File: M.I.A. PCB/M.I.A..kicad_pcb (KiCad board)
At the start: 4 copper layers, 50.8 x 106.6 mm, 177 parts, among them J1 USB_C_Receptacle_USB2.0_16P, J10 Conn_01x03, J11 Conn_01x03, J12 Screw_Terminal_01x02, J13 Screw_Terminal_01x02, J14 Screw_Terminal_01x02, J15 Screw_Terminal_01x02, J16 Screw_Terminal_01x02, J17 Screw_Terminal_01x02, J18 Screw_Terminal_01x02, J19 Conn_01x08_Socket, J2 Conn_01x02_Pin, J20 Screw_Terminal_01x02, J21 Conn_01x04_Socket, J22 Conn_01x04_Socket, J23 Conn_01x04_Socket, J24 Conn_01x04_Socket, J25 Conn_01x04_Socket, J26 Conn_01x02_Socket, J27 Conn_01x02_Socket, J28 Conn_01x02_Socket, J29 Conn_01x02_Socket, J3 Conn_01x03, J30 Conn_01x04_Socket, J31 Conn_01x04_Socket, J32 Conn_01x04_Socket, J33 Conn_Coaxial, J4 Conn_01x03, J5 Conn_01x03, J6 Conn_01x03, J7 MSD-4-A, J8 Conn_01x03, J9 Conn_01x03, Q1 AO3400A, Q2 AO3400A, Q3 AO3400A, Q4 AO3400A, SW1 SW_Push, SW2 SW_Push, U1 W25Q128JVS, U10 AP2112K-3.3, U11 INA219AxDCN, U12 AP62150WU, U13 TPS2121RUXR, U14 AP62150WU, U15 74AHC541, U2 RP2350B-QFN80, U3 MMC5983MA, U4 ICM-45686, U5 MS5611-01BA, U6 TMP117xxDRV, U7 MAX-M10S, U8 KX134-1211, U9 TPS2121RUXR, Y1 ABM8-272-T3

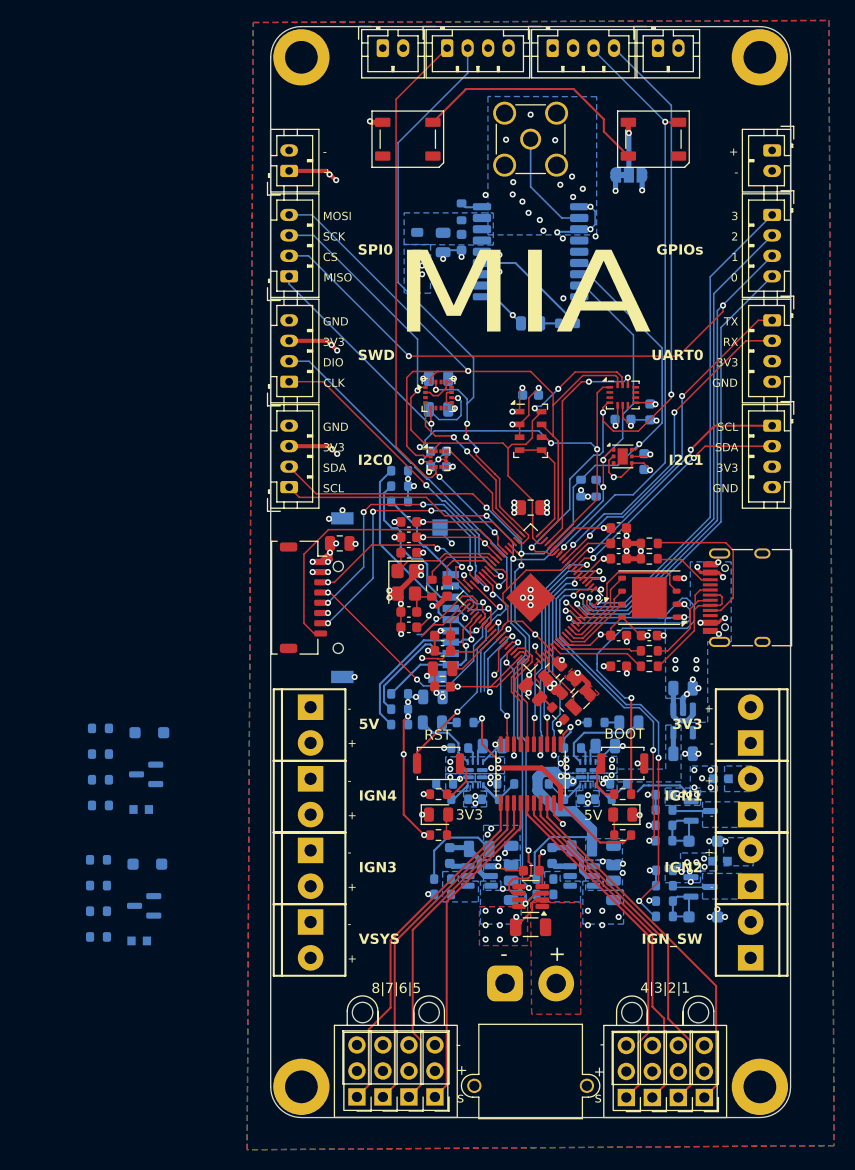
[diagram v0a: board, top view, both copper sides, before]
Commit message: Updated top connectors to be TLM_SPI
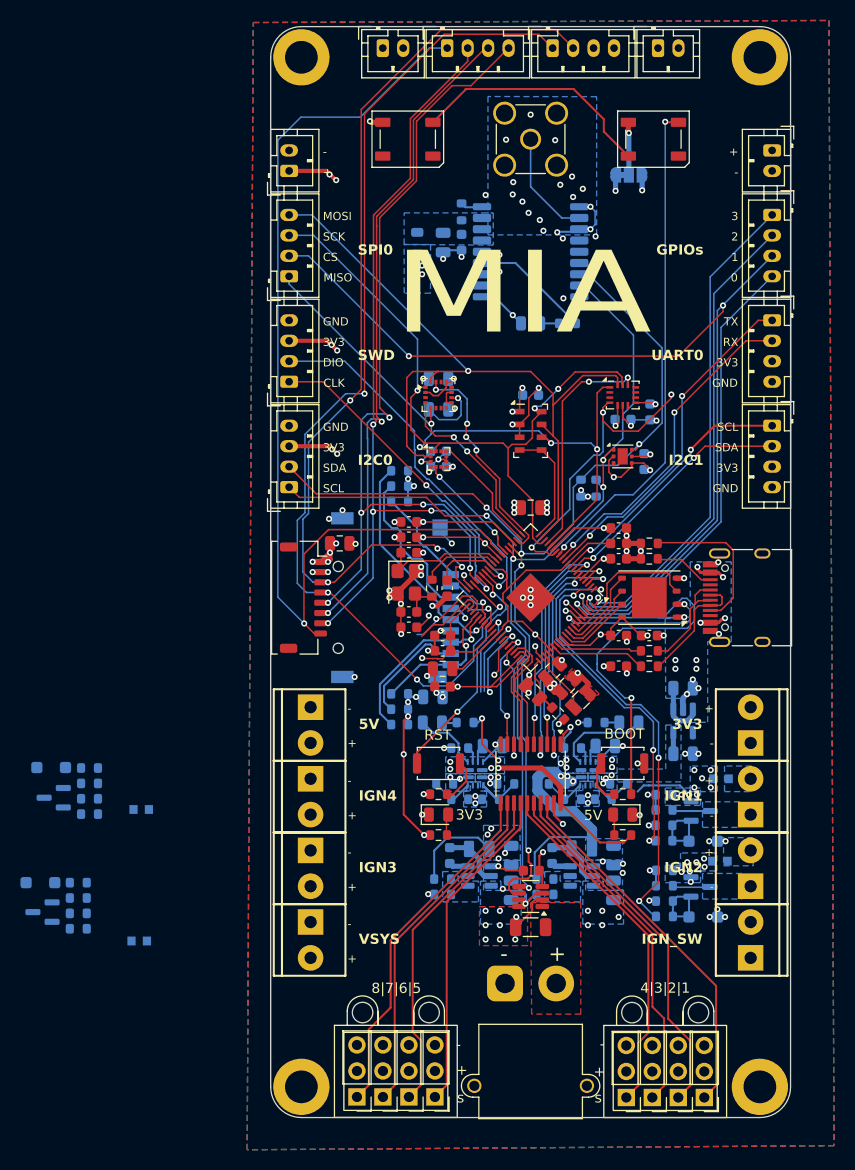
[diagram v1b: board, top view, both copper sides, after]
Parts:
- moved D9 10.6 mm to (-2.50, 98.7)
- moved D7 10.2 mm to (-1.45, 87.4)
- moved Q4 9.95 mm to (-2.30, 101.5)
- moved Q2 9.31 mm to (-1.20, 90.3)
- moved R39 6.96 mm to (2.30, 90.5), turned to 0 degrees
- moved R47 5.59 mm to (1.20, 101.7), turned to 0 degrees
- moved R52 2.36 mm to (1.20, 100.2)
- moved R53 2.13 mm to (1.20, 103.2)
- moved R49 1.99 mm to (1.20, 98.7)
- moved R41 1.73 mm to (2.30, 87.5)
- moved R45 1.36 mm to (2.30, 92.0)
- moved R44 1.13 mm to (2.30, 89.0)
- renumbered C22 to C20, C20 to C21, C23 to C22, C21 to C23, C41 to C25, C42 to C26, C43 to C27, C25 to C28, C26 to C29, C27 to C30, C28 to C31, C29 to C32, C30 to C33, C31 to C34, C32 to C35, C33 to C36, C34 to C37, C35 to C38, C36 to C39, C37 to C40, C38 to C41, C39 to C42, C40 to C43, D8 to D1, D9 to D2, D7 to D3, D1 to D4, D2 to D5, D4 to D6, D5 to D7, D3 to D8, D6 to D9, F3 to F2, F2 to F3, J5 to J10, J6 to J11, J7 to J12, J22 to J13, J8 to J14, J9 to J15, J10 to J16, J11 to J17, J23 to J18, J25 to J19, J33 to J2, J12 to J20, J20 to J21, J13 to J22, J16 to J23, J32 to J24, J19 to J25, J30 to J26, J29 to J27, J31 to J28, J28 to J29, J14 to J3, J27 to J30, J26 to J31, J15 to J32, J17 to J33, J18 to J4, J2 to J5, J24 to J6, J3 to J7, J4 to J8, J21 to J9, JP2 to JP1, Q3 to Q2, Q2 to Q3, R8 to R10, R9 to R11, R10 to R12, R51 to R13, R50 to R14, R11 to R15, R12 to R16, R13 to R17, R14 to R18, R16 to R19, R15 to R20, R17 to R21, R19 to R22, R18 to R23, R20 to R24, R21 to R25, R22 to R26, R23 to R27, R24 to R28, R25 to R29, R26 to R30, R27 to R31, R28 to R32, R29 to R33, R30 to R34, R31 to R35, R32 to R36, R33 to R37, R36 to R38, R42 to R39, R52 to R4, R34 to R40, R43 to R41, R35 to R42, R37 to R43, R38 to R46, R46 to R47, R39 to R48, R47 to R49, R4 to R5, R40 to R50, R41 to R51, R48 to R52, R49 to R53, R53 to R6, R5 to R7, R6 to R8, R7 to R9, U11 to U10, U10 to U11
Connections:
- J24 pad 1: GND -> SPI_SCK_TLM
- J24 pad 2: +3.3V -> D0_TLM
- J24 pad 3: LEDs -> GND
- J24 pad 4: IMU_INT1 -> +3.3V
- J28 pad 1: ACC_INT -> RST_TLM
- J28 pad 2: MAG_INT -> SPI_CS_TLM
- J28 pad 3: +3.3V -> SPI_MOSI_TLM
- J28 pad 4: GND -> SPI_MISO_TLM
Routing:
- net SPI_SCK_TLM: track 29.7 -> 105.0 mm, vias 3 -> 4
- net D0_TLM: track 19.5 -> 94.6 mm, vias 3 -> 4
- net RST_TLM: track 30.3 -> 98.9 mm, vias 0 -> 1
- net SPI_MOSI_TLM: track 16.9 -> 80.3 mm, vias 2 -> 3
- net SPI_MISO_TLM: track 30.6 -> 85.6 mm, vias 4 -> 5
- net SPI_CS_TLM: track 28.7 -> 78.0 mm, vias 4 -> 5
- net ACC_INT: track 57.5 -> 11.1 mm
- net MAG_INT: track 63.1 -> 22.2 mm
- net IMU_INT1: track 66.4 -> 30.2 mm
- net LEDs: track 59.2 -> 49.1 mm
- net SWDIO: track 34.6 -> 36.5 mm

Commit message: routed ign3/4, fixed some drc
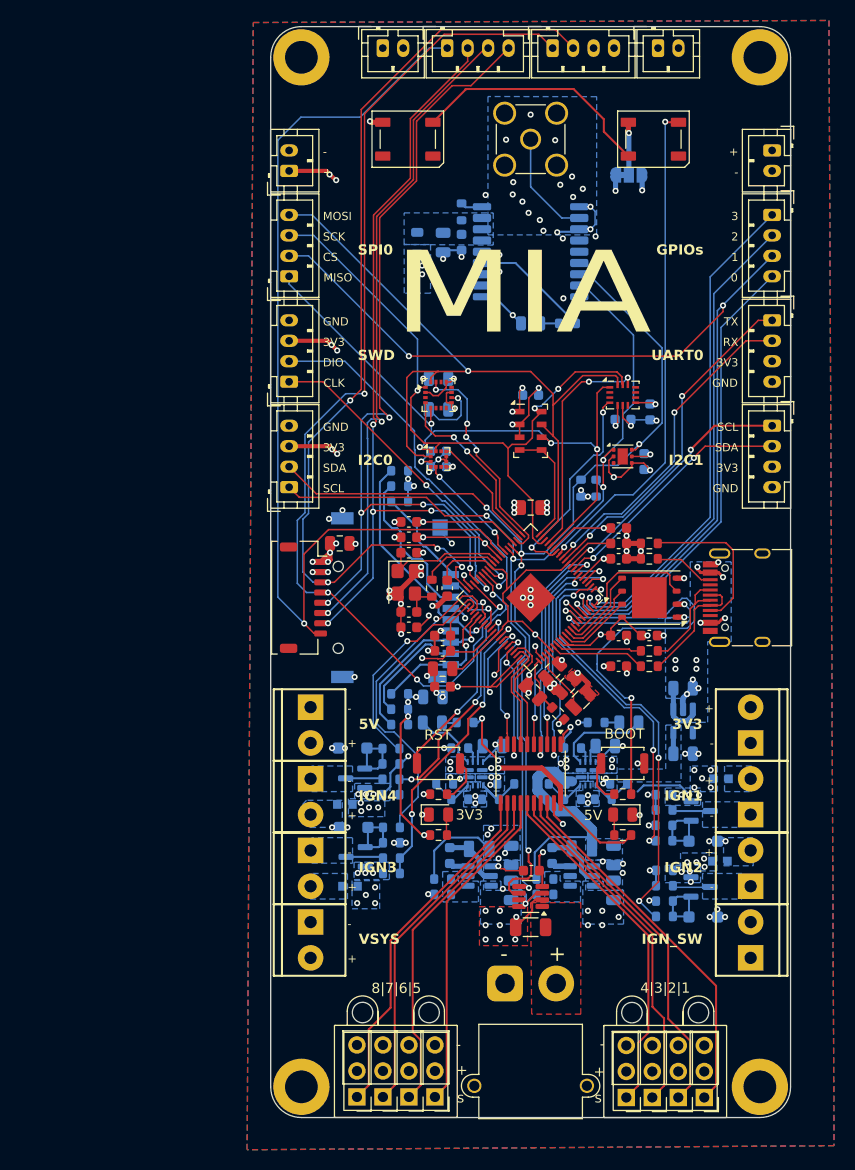
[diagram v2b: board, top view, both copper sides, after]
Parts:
- moved D9 31.1 mm to (28.1, 93.2)
- moved Q4 31.1 mm to (28.3, 96.1)
- moved R47 31.1 mm to (31.8, 96.2)
- moved R49 31.1 mm to (31.8, 93.2)
- moved R52 31.1 mm to (31.8, 94.8)
- moved R53 31.1 mm to (31.8, 97.8)
- moved D7 29.5 mm to (28.0, 85.5)
- moved Q2 29.5 mm to (28.2, 88.5)
- moved R39 29.5 mm to (31.8, 88.5)
- moved R41 29.5 mm to (31.8, 85.5)
- moved R44 29.5 mm to (31.8, 87.0)
- moved R45 29.5 mm to (31.8, 90.0)
- moved F4 21.3 mm to (27.8, 99.0), turned to 0 degrees
- moved F2 19.9 mm to (27.2, 91.0), turned to 0 degrees
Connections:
- U2 pad 49: Cont_Sense4 -> Cont_Sense3
- U2 pad 52: Cont_Sense3 -> Cont_Sense4
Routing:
- net IGN_4: track 9.30 -> 32.3 mm
- net Cont_Sense4: track 8.68 -> 29.5 mm, vias 1 -> 3
- net Cont_Sense3: track 8.31 -> 23.0 mm, vias 1 -> 3
- net IGN_3: track 7.66 -> 22.1 mm, vias 0 -> 1
- net IMU_INT1: track 30.2 -> 20.6 mm, vias 3 -> 2
- net Net-(D7-K): track 0.00 -> 7.06 mm
- net Net-(D9-K): track 0.00 -> 6.93 mm
- net Net-(J33-Pin_1): track 0.00 -> 3.66 mm
- net Net-(J23-Pin_1): track 0.00 -> 3.65 mm
- net GND: track 138.2 -> 141.7 mm, vias 118 -> 130
- net GPIO1: track 97.4 -> 96.6 mm
- net +3.3V: track 173.4 -> 172.9 mm, vias 57 -> 56
- net V_IGN: vias 9 -> 17
- net 3.3v_usb: vias 3 -> 2
- net 3.3v_Batt: vias 3 -> 0
- added copper zone on B.Cu, net Net-(J23-Pin_1)
- added copper zone on B.Cu, net Net-(J23-Pin_2)
- added copper zone on B.Cu, net Net-(J33-Pin_1)
- added copper zone on B.Cu, net Net-(J33-Pin_2)
- removed copper zone on In1.Cu, net GND

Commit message: Final Fixes, impedances, silkscreen etc
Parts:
- added REF**: orientationIndicator, Graphics:orientationIndicator, F.Cu at (36.1, 101.6)
- R2, R3: value 22 -> 27
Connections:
- J24 pad 1: SPI_SCK_TLM -> RST_TLM
- J28 pad 1: RST_TLM -> SPI_MISO_TLM
- J28 pad 3: SPI_MOSI_TLM -> SPI_SCK_TLM
- J28 pad 4: SPI_MISO_TLM -> SPI_MOSI_TLM
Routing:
- net RST_TLM: track 98.9 -> 109.7 mm
- net +5V_USB: track 37.2 -> 46.4 mm, vias 11 -> 10
- net SPI_SCK_TLM: track 105.0 -> 96.5 mm
- net /D+: track 10.8 -> 16.6 mm
- net +3.3V: track 172.9 -> 176.7 mm, vias 56 -> 55
- net GND: track 141.7 -> 145.3 mm, vias 130 -> 146
- net SPI_MOSI_TLM: track 80.2 -> 76.9 mm
- net SPI_CS_TLM: track 77.9 -> 79.2 mm
- net 3.3v_usb: vias 2 -> 0
- added copper zone on In1.Cu, net GND
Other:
- board text added: "27"
- board text added: "32"
- board text added: "DI"
- board text added: "DO"
- board text added: "GPS"

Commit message: More Small Updates/Improvements
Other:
- board text added: "Batt 3V3"
- board text added: "Batt 5V"
- board text added: "SRC 3V3"
- board text added: "SRC 5V"
- board text added: "USB 3V3"
- board text added: "USB 5V"
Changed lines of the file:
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@@
 			(at 0 1.635 0)
 			(layer "B.SilkS")
+			(hide yes)
 			(effects
 				(font
@@
 		)
 	)
+	(gr_line
+		(start 59.4 78.175)
+		(end 59.4 78.525)
+		(stroke
+			(width 0.1)
+			(type default)
+		)
+		(layer "B.SilkS")
+	)
+	(gr_line
+		(start 41.35 94.15)
+		(end 41.35 94.5)
+		(stroke
+			(width 0.1)
+			(type default)
+		)
+		(layer "B.SilkS")
+	)
+	(gr_line
+		(start 51.45 93.9)
+		(end 51.45 94.25)
+		(stroke
+			(width 0.1)
+			(type default)
+		)
+		(layer "B.SilkS")
+	)
+	(gr_line
+		(start 59.3 86.9)
+		(end 59.3 87.25)
+		(stroke
+			(width 0.1)
+			(type default)
+		)
+		(layer "B.SilkS")
+	)
 	(gr_arc
 		(start 20 18)
@@
 		)
 	)
+	(gr_text "3V3"
+		(at 52.95 30.1 0)
+		(layer "B.SilkS")
+		(effects
+			(font
+				(size 1 1)
+				(thickness 0.1)
+			)
+			(justify left bottom mirror)
+		)
+	)
+	(gr_text "Batt 5V"
+		(at 44.7 94 0)
+		(layer "B.SilkS")
+		(effects
+			(font
+				(size 1 1)
+				(thickness 0.15)
+			)
+			(justify left bottom mirror)
+		)
+	)
+	(gr_text "Batt 3V3"
+		(at 54.8 93.75 0)
+		(layer "B.SilkS")
+		(effects
+			(font
+				(size 1 1)
+				(thickness 0.15)
+			)
+			(justify left bottom mirror)
+		)
+	)
+	(gr_text "5V"
+		(at 59.05 30.15 0)
+		(layer "B.SilkS")
+		(effects
+			(font
+				(size 1 1)
+				(thickness 0.1)
+			)
+			(justify left bottom mirror)
+		)
+	)
+	(gr_text "SRC 5V"
+		(at 43.35 81.85 0)
+		(layer "B.SilkS")
+		(effects
+			(font
+				(size 1 1)
+				(thickness 0.15)
+			)
+			(justify left bottom mirror)
+		)
+	)
+	(gr_text "USB 3V3"
+		(at 62.8 88.6 0)
+		(layer "B.SilkS")
+		(effects
+			(font
+				(size 1 1)
+				(thickness 0.15)
+			)
+			(justify left bottom mirror)
+		)
+	)
+	(gr_text "SRC 3V3"
+		(at 58.55 81.8 0)
+		(layer "B.SilkS")
+		(effects
+			(font
+				(size 1 1)
+				(thickness 0.15)
+			)
+			(justify left bottom mirror)
+		)
+	)
+	(gr_text "USB 5V"
+		(at 62.9 78.15 0)
+		(layer "B.SilkS")
+		(effects
+			(font
+				(size 1 1)
+				(thickness 0.15)
+			)
+			(justify left bottom mirror)
+		)
+	)
